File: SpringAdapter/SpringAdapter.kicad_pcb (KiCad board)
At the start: 2 copper layers, 32 x 32.1 mm, 18 parts, among them J1 USB_C_Receptacle_USB2.0, J2 Conn_02x04_Odd_Even, SW1 SW_DIP_x01, U1 AP2112K-3.3

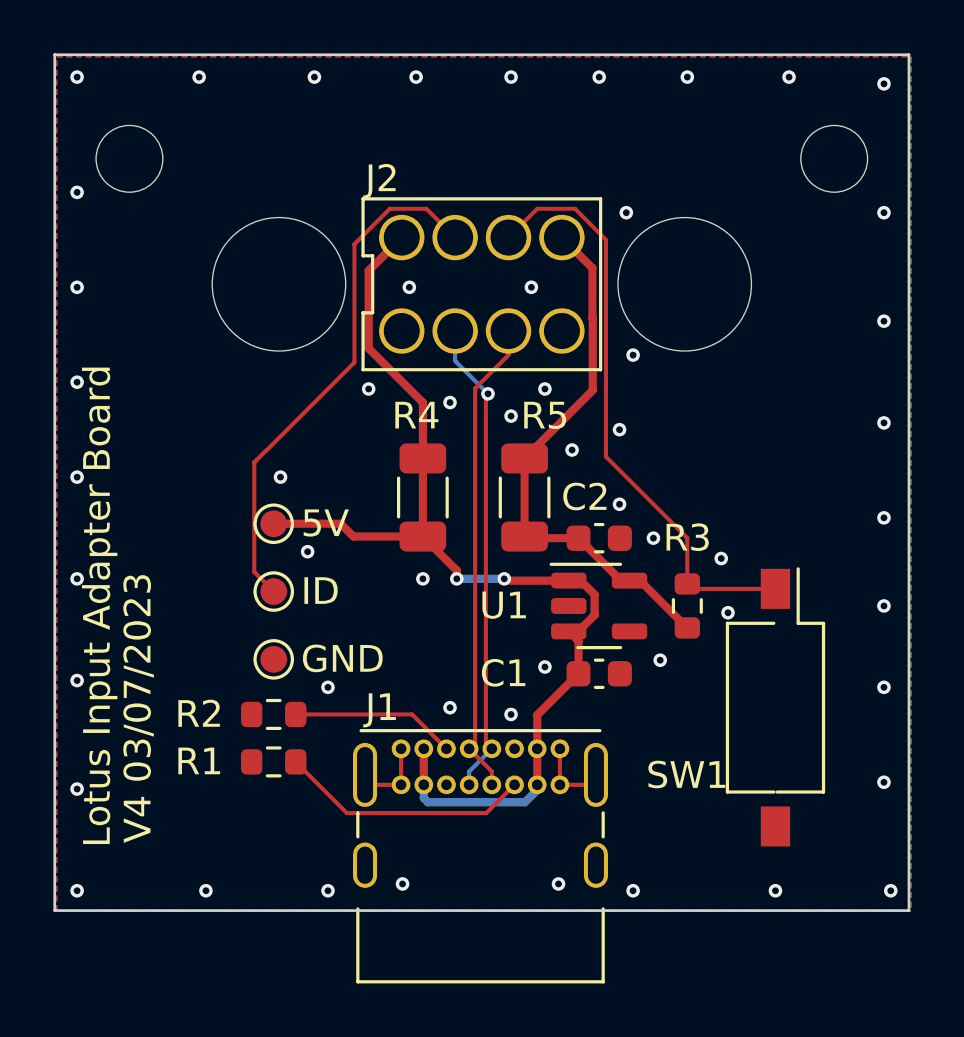
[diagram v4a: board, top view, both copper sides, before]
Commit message: Add bosses to pogo connector
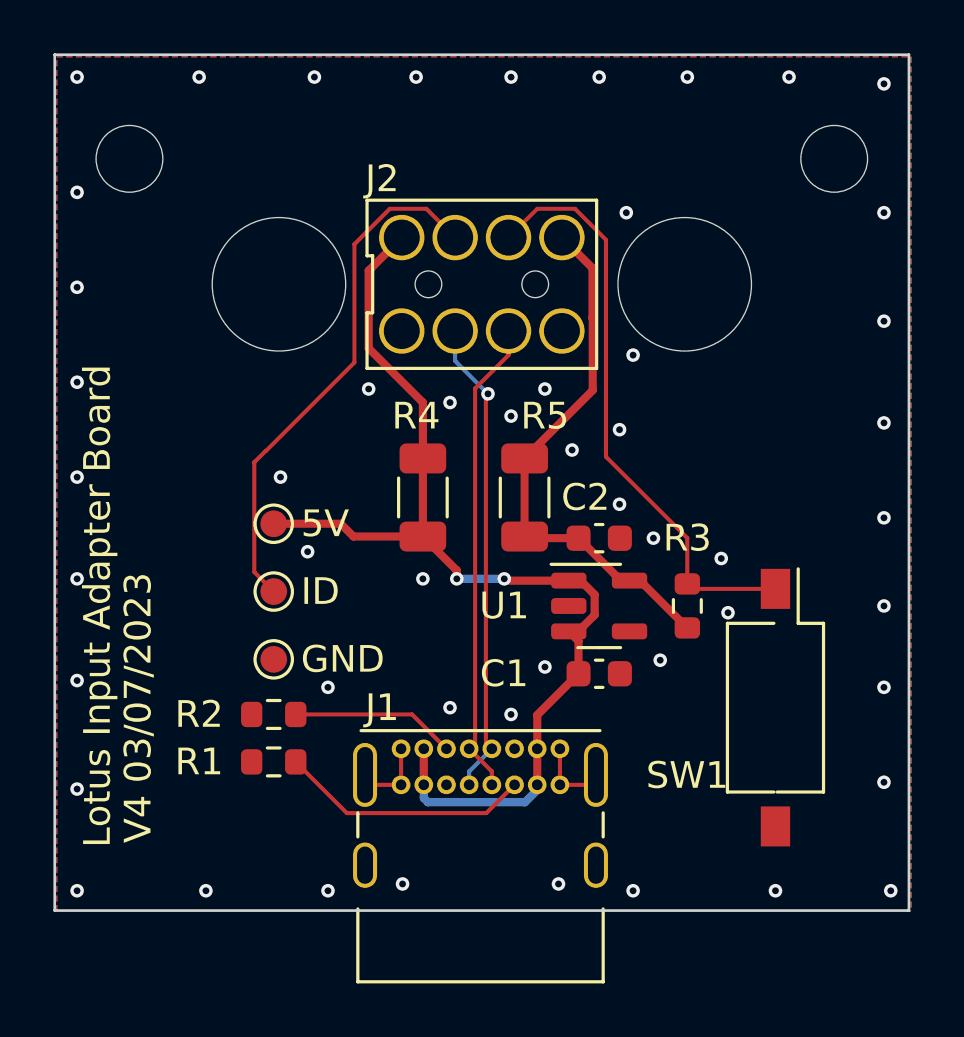
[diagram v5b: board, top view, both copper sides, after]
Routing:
- net GND: vias 53 -> 51
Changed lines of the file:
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@@
       (outputformat 1)
       (mirror false)
-      (drillshape 1)
+      (drillshape 0)
       (scaleselection 1)
-      (outputdirectory "")
+      (outputdirectory "C:/Users/nrp/Downloads/springadapter_gerbers/")
     )
   )
@@
         (effects (font (size 1 1) (thickness 0.15)))
     )
-    (fp_line (start -4.45 -3.2) (end -4.45 -1.066666)
+    (fp_line (start -4.3 -3.15) (end -4.3 -1.066666)
       (stroke (width 0.12) (type default)) (layer "F.SilkS"))
-    (fp_line (start -4.45 -1.066666) (end -4.09 -1.066666)
+    (fp_line (start -4.3 -1.066666) (end -4.09 -1.066666)
       (stroke (width 0.12) (type default)) (layer "F.SilkS"))
-    (fp_line (start -4.45 1.066666) (end -4.45 3.199999)
+    (fp_line (start -4.3 1.066666) (end -4.3 3.15)
       (stroke (width 0.12) (type default)) (layer "F.SilkS"))
-    (fp_line (start -4.45 3.199999) (end 4.45 3.2)
+    (fp_line (start -4.3 3.15) (end 4.3 3.15)
       (stroke (width 0.12) (type default)) (layer "F.SilkS"))
     (fp_line (start -4.09 -1.066666) (end -4.09 1.066666)
       (stroke (width 0.12) (type default)) (layer "F.SilkS"))
-    (fp_line (start -4.09 1.066666) (end -4.45 1.066666)
+    (fp_line (start -4.09 1.066666) (end -4.3 1.066666)
       (stroke (width 0.12) (type default)) (layer "F.SilkS"))
-    (fp_line (start 4.45 -3.199999) (end -4.45 -3.2)
+    (fp_line (start 4.3 -3.15) (end -4.3 -3.15)
       (stroke (width 0.12) (type default)) (layer "F.SilkS"))
-    (fp_line (start 4.45 3.2) (end 4.45 -3.199999)
+    (fp_line (start 4.3 3.15) (end 4.3 -3.15)
       (stroke (width 0.12) (type default)) (layer "F.SilkS"))
     (fp_line (start -4.55 -3.4) (end 4.55 -3.4)
@@
     (fp_line (start 4.55 3.4) (end -4.55 3.4)
       (stroke (width 0.05) (type default)) (layer "F.CrtYd"))
+    (pad "" np_thru_hole circle (at -2 0) (size 1 1) (drill 1) (layers "*.Mask"))
+    (pad "" np_thru_hole circle (at 2 0) (size 1 1) (drill 1) (layers "*.Mask"))
     (pad "1" thru_hole circle (at -3 1.75) (size 1.7 1.7) (drill 1.35) (layers "*.Cu" "*.Mask")
       (net 2 "GND") (pinfunction "Pin_1") (pintype "passive"))
@@
     (fp_line (start 1.6 0.8) (end -1.6 0.8)
       (stroke (width 0.1) (type solid)) (layer "F.Fab"))
-    (pad "1" smd roundrect (at -1.4625 0 90) (size 1.125 1.75) (layers "F.Cu" "F.Paste" "F.Mask") (roundrect_rratio 0.222222)
+    (pad "1" smd roundrect (at -1.4625 0 90) (size 1.125 1.75) (layers "F.Cu" "F.Paste" "F.Mask") (roundrect_rratio 0.2222222222)
       (net 1 "+5V") (pintype "passive"))
-    (pad "2" smd roundrect (at 1.4625 0 90) (size 1.125 1.75) (layers "F.Cu" "F.Paste" "F.Mask") (roundrect_rratio 0.222222)
+    (pad "2" smd roundrect (at 1.4625 0 90) (size 1.125 1.75) (layers "F.Cu" "F.Paste" "F.Mask") (roundrect_rratio 0.2222222222)
       (net 1 "+5V") (pintype "passive"))
     (model "${KICAD6_3DMODEL_DIR}/Resistor_SMD.3dshapes/R_1206_3216Metric.wrl"
@@
     (fp_line (start 1.6 0.8) (end -1.6 0.8)
       (stroke (width 0.1) (type solid)) (layer "F.Fab"))
-    (pad "1" smd roundrect (at -1.4625 0 90) (size 1.125 1.75) (layers "F.Cu" "F.Paste" "F.Mask") (roundrect_rratio 0.222222)
+    (pad "1" smd roundrect (at -1.4625 0 90) (size 1.125 1.75) (layers "F.Cu" "F.Paste" "F.Mask") (roundrect_rratio 0.2222222222)
       (net 3 "+3.3V") (pintype "passive"))
-    (pad "2" smd roundrect (at 1.4625 0 90) (size 1.125 1.75) (layers "F.Cu" "F.Paste" "F.Mask") (roundrect_rratio 0.222222)
+    (pad "2" smd roundrect (at 1.4625 0 90) (size 1.125 1.75) (layers "F.Cu" "F.Paste" "F.Mask") (roundrect_rratio 0.2222222222)
       (net 3 "+3.3V") (pintype "passive"))
     (model "${KICAD6_3DMODEL_DIR}/Resistor_SMD.3dshapes/R_1206_3216Metric.wrl"
@@
   (via (at 118.872 131.064) (size 0.508) (drill 0.254) (layers "F.Cu" "B.Cu") (free) (net 2))
   (via (at 120.396 100.838) (size 0.508) (drill 0.254) (layers "F.Cu" "B.Cu") (free) (net 2))
-  (via (at 117.856 108.712) (size 0.508) (drill 0.254) (layers "F.Cu" "B.Cu") (free) (net 2))
   (via (at 113.792 119.634) (size 0.508) (drill 0.254) (layers "F.Cu" "B.Cu") (free) (net 2))
   (via (at 131.064 113.792) (size 0.508) (drill 0.254) (layers "F.Cu" "B.Cu") (free) (net 2))
   (via (at 118.364 122.936) (size 0.508) (drill 0.254) (layers "F.Cu" "B.Cu") (free) (net 2))
-  (via (at 113.284 108.712) (size 0.508) (drill 0.254) (layers "F.Cu" "B.Cu") (free) (net 2))
   (via (at 127 131.318) (size 0.508) (drill 0.254) (layers "F.Cu" "B.Cu") (free) (net 2))
   (via (at 131.064 120.65) (size 0.508) (drill 0.254) (layers "F.Cu" "B.Cu") (free) (net 2))
